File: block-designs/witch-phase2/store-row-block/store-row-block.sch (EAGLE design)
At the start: 15 parts, among them IC2 74LVC1G125DBV, Q1 MMBT2907ALT1SMD

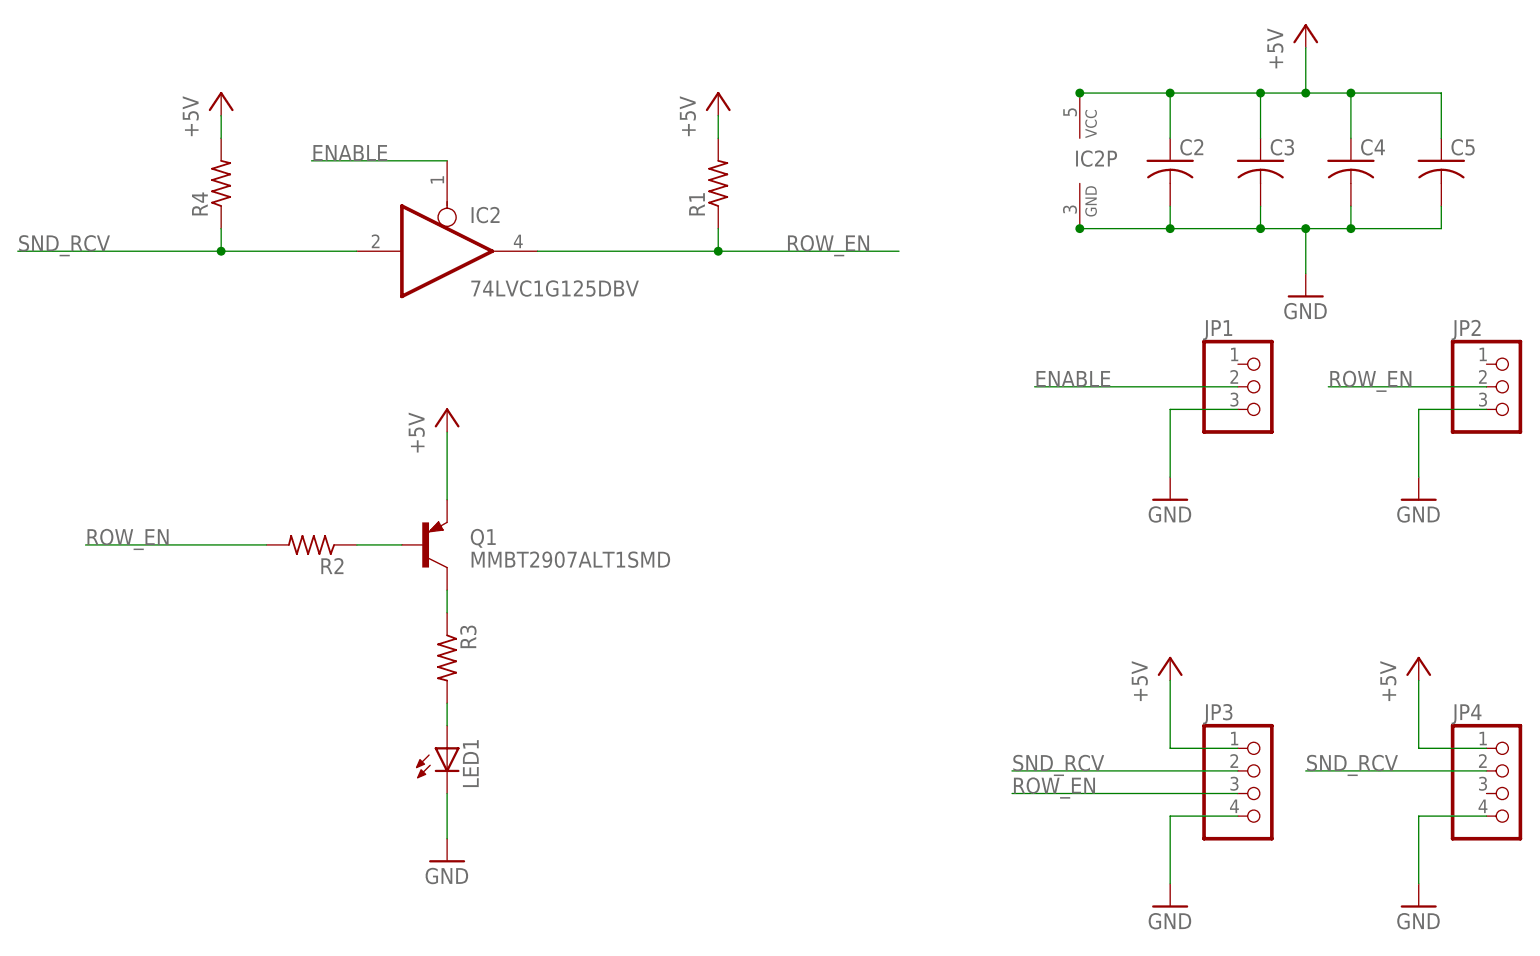
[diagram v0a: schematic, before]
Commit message: updated revisions with fixes for manufacturing
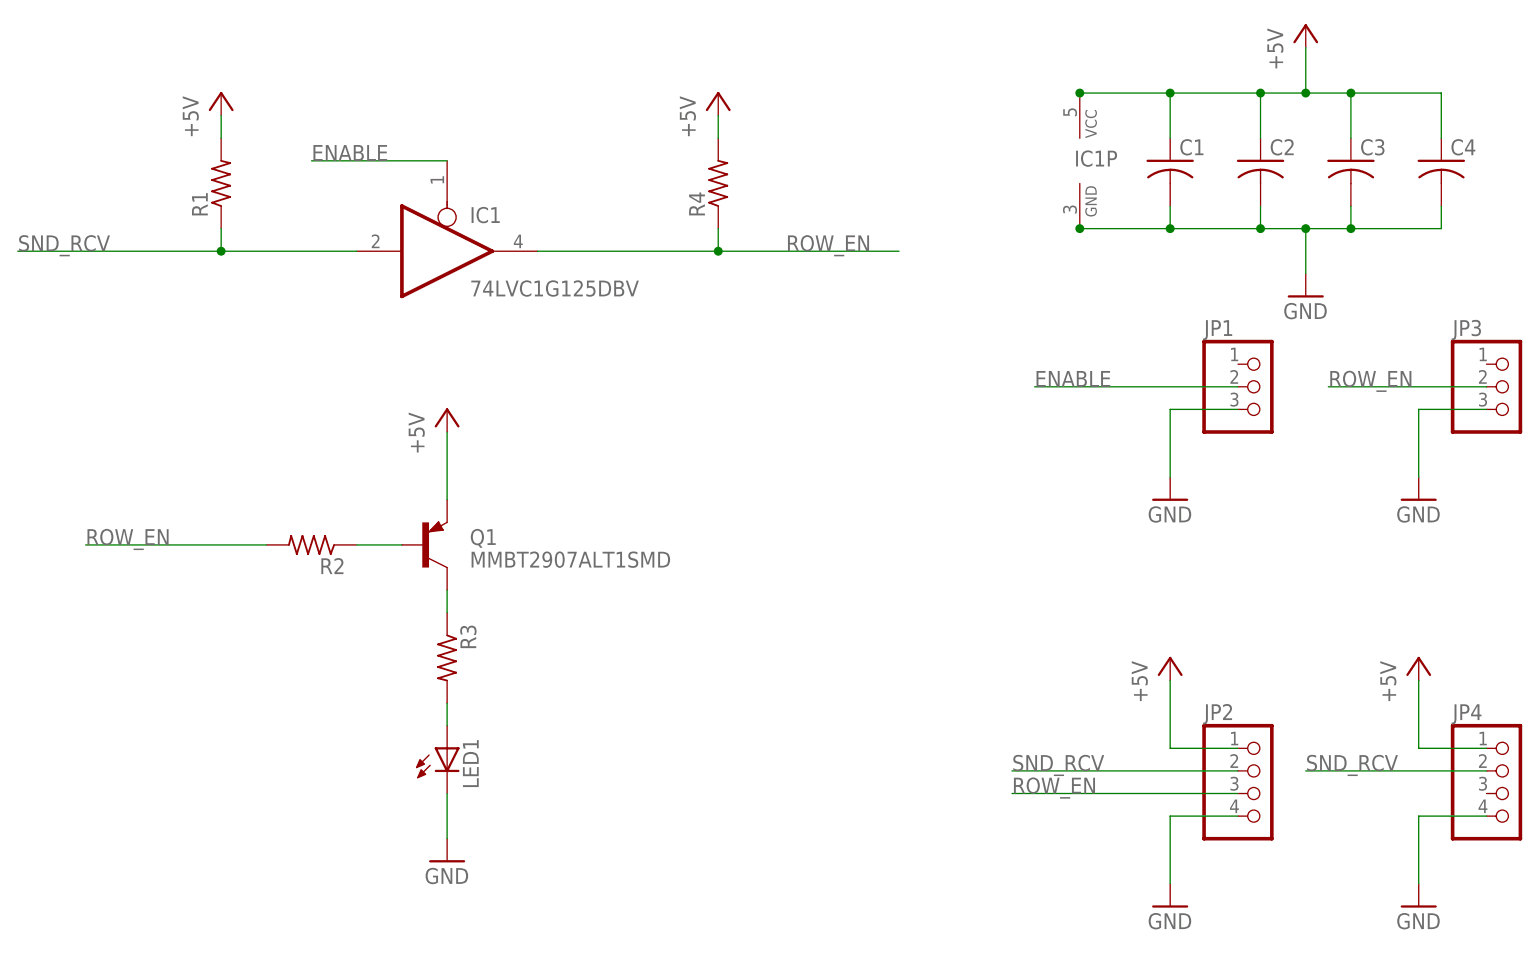
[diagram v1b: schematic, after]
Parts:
- removed C5: (no value), resistor:C-USC0805
- added C1: (no value), resistor:C-USC0805
- JP2: device pinhead:PINHD-1X3 -> pinhead:PINHD-1X4
- JP3: device pinhead:PINHD-1X4 -> pinhead:PINHD-1X3
- renumbered IC2 to IC1
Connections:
- net +5V: now also C1.1, JP2.1; no longer C5.1, JP3.1
- net GND: now also C1.2, JP2.4, JP3.3; no longer C5.2, JP2.3, JP3.4
- net ROW_EN: now also JP2.3, JP3.2, R4.1; no longer JP2.2, JP3.3, R1.1
- net SND_RCV: now also JP2.2, R1.1; no longer JP3.2, R4.1
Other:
- moved on the sheet: C2, C3, C4, R1, R4
